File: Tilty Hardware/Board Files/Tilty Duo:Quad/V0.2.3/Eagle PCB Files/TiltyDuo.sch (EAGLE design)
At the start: 39 parts, among them U1 TEENSY_3.0_OUTER-PINS28-DIP_S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, U2 HC-09_BREAKOUT, U3 MPL3115A2LGA8, U4 LM2931, U5 MPU-6050, U6 HMC5883LSMD, U7 24LC08BT

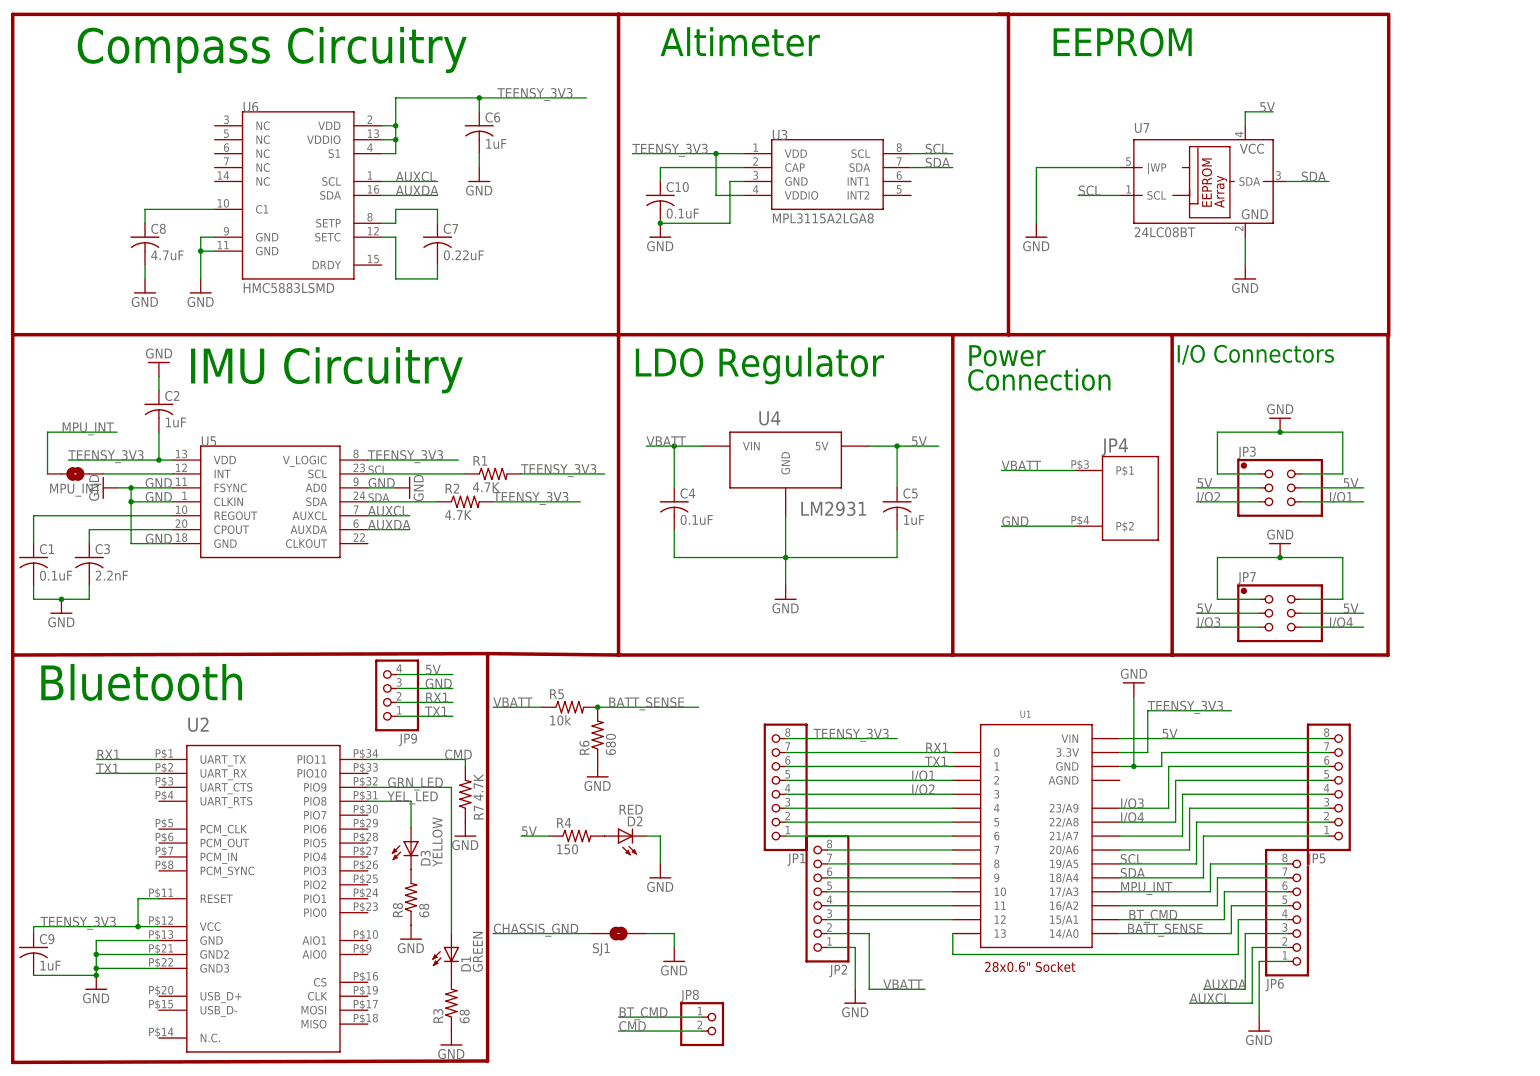
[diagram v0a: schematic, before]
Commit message: PCB hardware update
Tilty Duo/Quad v0.2.3 PCB added with minor changes.
Tilty Quad BOM updated for v0.2.2
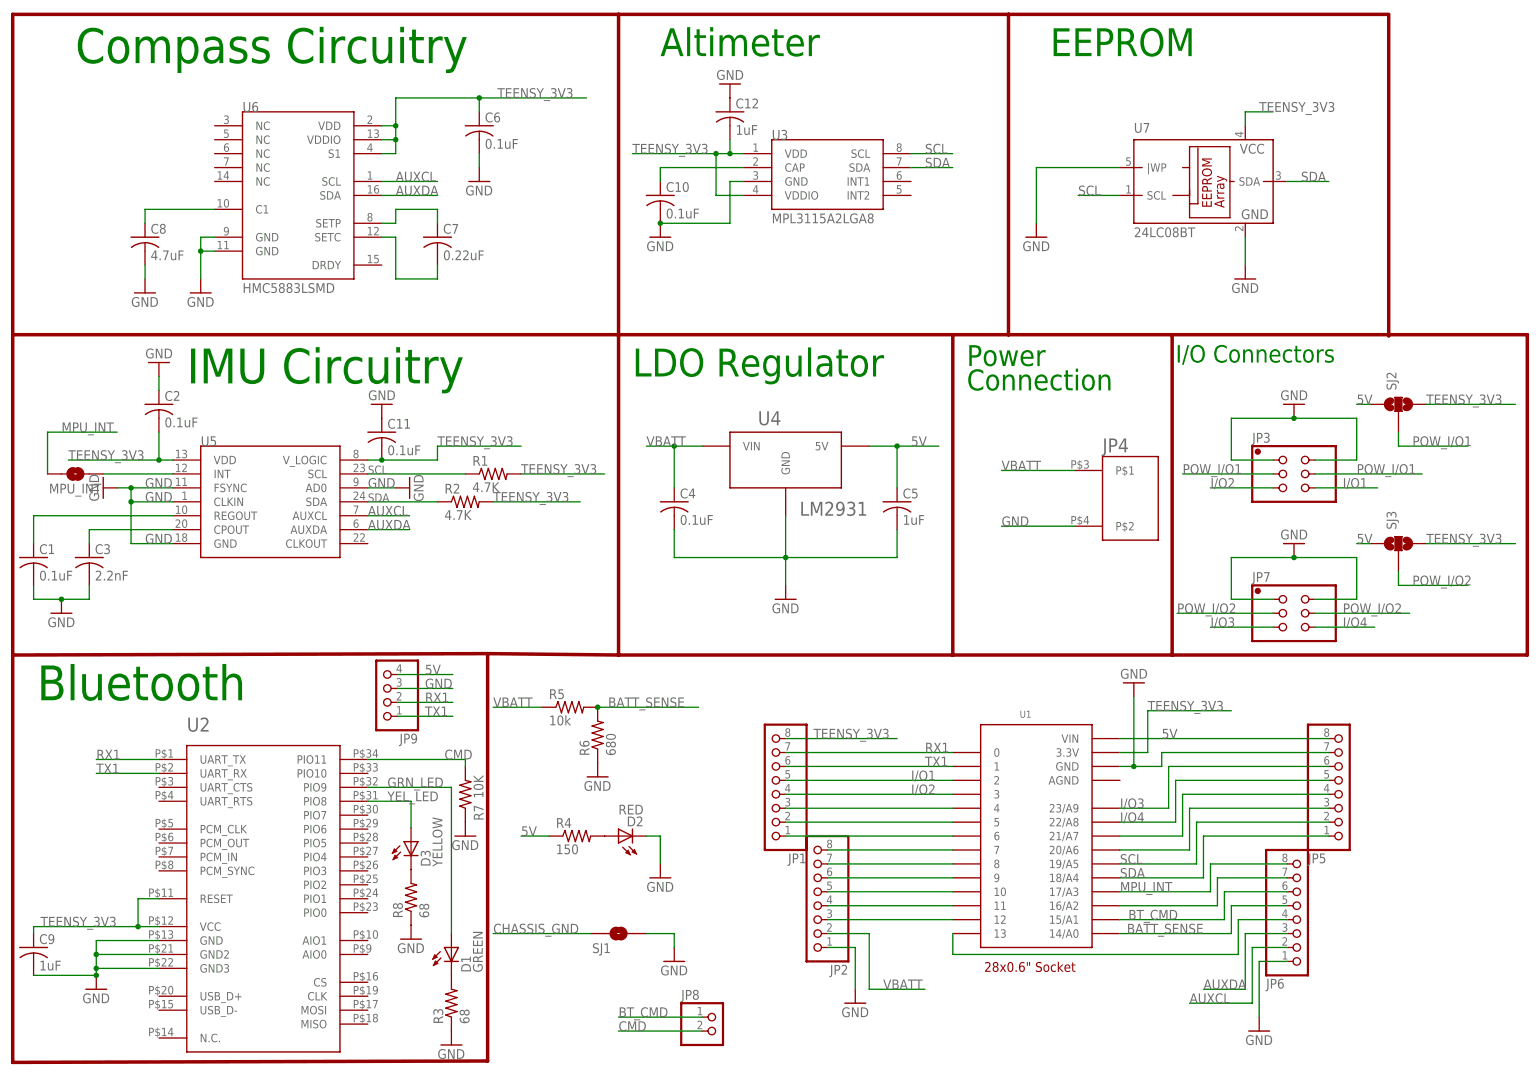
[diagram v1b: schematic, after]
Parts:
- added C11: 0.1uF, resistor:C-USC0603
- added C12: 1uF, resistor:C-USC0603
- added SJ2, SJ3: (no value), SparkFun-Passives:SOLDERJUMPER_2WAYS
- C2, C6: value 1uF -> 0.1uF
- C7, C8: ESR (none) -> <200mOhms
- R1, R2: device resistor:R-US_R0402 -> resistor:R-US_R0603
- R7: value 4.7K -> 10K
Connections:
- new net POW_I/O1: JP3.3, JP3.4, SJ2.2
- new net POW_I/O2: JP7.3, JP7.4, SJ3.2
- net 5V: now also SJ2.1, SJ3.1; no longer JP3.3, JP3.4, JP7.3, JP7.4, U7.VCC
- net GND: now also C11.1, C12.1
- net TEENSY_3V3: now also C11.2, C12.2, SJ2.3, SJ3.3, U7.VCC
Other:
- moved on the sheet: JP3, JP7

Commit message: Updated dual motor driver and Tilty Duo/Quad PCBs, added a copuple experimental arduino programs
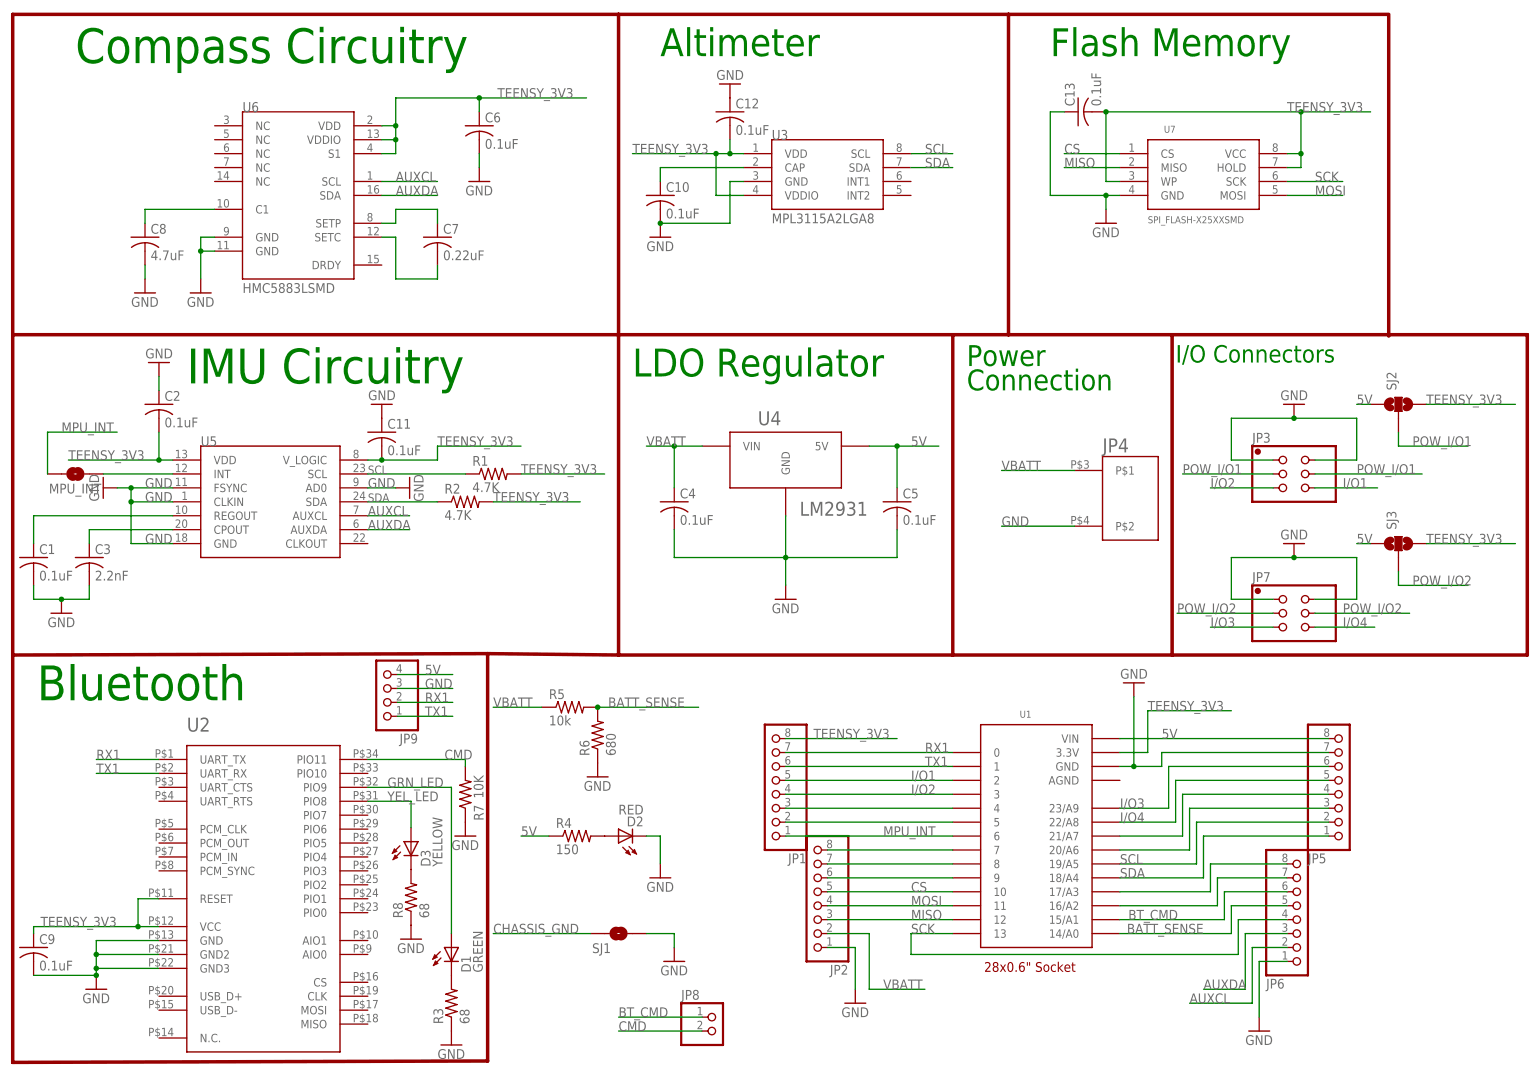
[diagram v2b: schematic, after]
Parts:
- added C13: 0.1uF, resistor:C-USC0603
- C12, C5, C9: value 1uF -> 0.1uF
- JP1, JP2, JP5, JP6: device pinhead:PINHD-1X81X08_NO_SILK -> pinhead:PINHD-1X81X08_NO_SILK_LOCK
- JP3, JP7: device pinhead:PINHD-2X32X03_NO_SILK -> pinhead:PINHD-2X32X03_NO_SS_LOCK
- U7: value 24LC08BT -> SPI_FLASH-X25XXSMD; device microchip:24LC08BT -> SparkFun-DigitalIC:SPI_FLASH-X25XXSMD; PART# (none) -> S25FL204K0TMFI011; PART#2 (none) -> S25FL208K0RMFI011
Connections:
- removed net N$13: JP2.5, U1.10
- removed net N$14: JP2.4, U1.11
- removed net N$15: JP2.3, U1.12
- removed net N$9: JP1.1, U1.6
- new net CS: JP2.5, U1.10, U7.CS
- new net MISO: JP2.3, U1.12, U7.MISO
- new net MOSI: JP2.4, U1.11, U7.MOSI
- new net SCK: JP6.4, U1.13, U7.SCK
- net GND: now also C13.1; no longer U7.|WP
- net MPU_INT: now also JP1.1, U1.6; no longer JP6.8, U1.17/A3
- net N$10: now also JP6.8, U1.17/A3; no longer JP6.4, U1.13
- net SCL: no longer U7.SCL
- net SDA: no longer U7.SDA
- net TEENSY_3V3: now also C13.2, U7.HOLD, U7.WP
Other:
- note added: "Flash Memory"
- note removed: "EEPROM"

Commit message: Slightly improved Tilty Duo/Quad PCB traces
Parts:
- JP9: device pinhead:PINHD-1X4 -> pinhead:PINHD-1X41X04_NO_SS_LOCKING
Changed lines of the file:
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@@
 <setting verticaltext="up"/>
 </settings>
-<grid distance="0.1" unitdist="inch" unit="inch" style="lines" multiple="1" display="no" altdistance="0.01" altunitdist="inch" altunit="inch"/>
+<grid distance="0.05" unitdist="inch" unit="inch" style="lines" multiple="1" display="no" altdistance="0.01" altunitdist="inch" altunit="inch"/>
 <layers>
 <layer number="1" name="Top" color="4" fill="1" visible="no" active="no"/>
@@
 <part name="GND18" library="supply1" deviceset="GND" device=""/>
 <part name="JP8" library="pinhead" deviceset="PINHD-1X2" device="1X02_NO_SILK"/>
-<part name="JP9" library="pinhead" deviceset="PINHD-1X4" device=""/>
 <part name="GND19" library="supply1" deviceset="GND" device=""/>
 <part name="R7" library="resistor" deviceset="R-US_" device="R0603" value="10K"/>
@@
 <attribute name="RATED_VOLTAGE" value="2"/>
 </part>
+<part name="JP9" library="pinhead" deviceset="PINHD-1X4" device="1X04_NO_SS_LOCKING"/>
 </parts>
 <sheets>
@@
 <instance part="GND18" gate="1" x="121.92" y="20.32"/>
 <instance part="JP8" gate="G$1" x="129.54" y="7.62"/>
-<instance part="JP9" gate="A" x="68.834" y="70.104" rot="R180"/>
 <instance part="GND19" gate="1" x="83.82" y="43.18"/>
 <instance part="R7" gate="G$1" x="83.82" y="50.8" smashed="yes" rot="R90">
@@
 <attribute name="RATED_VOLTAGE" x="195.58" y="175.26" size="1.778" layer="96" rot="R90" display="off"/>
 </instance>
+<instance part="JP9" gate="A" x="68.834" y="70.104" rot="R180"/>
 </instances>
 <busses>
@@
 </segment>
 <segment>
-<pinref part="JP9" gate="A" pin="3"/>
 <wire x1="71.374" y1="70.104" x2="81.534" y2="70.104" width="0.1524" layer="91"/>
 <label x="76.454" y="70.104" size="1.778" layer="95"/>
+<pinref part="JP9" gate="A" pin="3"/>
 </segment>
 <segment>
@@
 </net>
 <net name="TEENSY_3V3" class="3">
-<segment>
-<pinref part="R1" gate="G$1" pin="2"/>
-<wire x1="93.98" y1="109.22" x2="109.22" y2="109.22" width="0.1524" layer="91"/>
-<label x="93.98" y="109.22" size="1.778" layer="95"/>
-<wire x1="78.74" y1="114.3" x2="93.98" y2="114.3" width="0.1524" layer="91"/>
-<label x="78.74" y="114.3" size="1.778" layer="95"/>
-</segment>
 <segment>
 <pinref part="R2" gate="G$1" pin="2"/>
@@
 <wire x1="66.04" y1="111.76" x2="68.58" y2="111.76" width="0.1524" layer="91"/>
 <wire x1="68.58" y1="111.76" x2="78.74" y2="111.76" width="0.1524" layer="91"/>
+<junction x="68.58" y="111.76"/>
+<pinref part="R1" gate="G$1" pin="2"/>
+<wire x1="93.98" y1="109.22" x2="109.22" y2="109.22" width="0.1524" layer="91"/>
+<label x="93.98" y="109.22" size="1.778" layer="95"/>
+<wire x1="78.74" y1="114.3" x2="93.98" y2="114.3" width="0.1524" layer="91"/>
+<label x="78.74" y="114.3" size="1.778" layer="95"/>
 <wire x1="78.74" y1="111.76" x2="78.74" y2="114.3" width="0.1524" layer="91"/>
-<junction x="68.58" y="111.76"/>
 </segment>
 <segment>
@@
 </segment>
 <segment>
-<pinref part="JP9" gate="A" pin="4"/>
 <wire x1="71.374" y1="72.644" x2="81.534" y2="72.644" width="0.1524" layer="91"/>
 <label x="76.454" y="72.644" size="1.778" layer="95"/>
+<pinref part="JP9" gate="A" pin="4"/>
 </segment>
 <segment>
@@
 </segment>
 <segment>
-<pinref part="JP9" gate="A" pin="2"/>
 <wire x1="71.374" y1="67.564" x2="81.534" y2="67.564" width="0.1524" layer="91"/>
 <label x="76.454" y="67.564" size="1.778" layer="95"/>
+<pinref part="JP9" gate="A" pin="2"/>
 </segment>
 </net>
@@
 </segment>
 <segment>
-<pinref part="JP9" gate="A" pin="1"/>
 <wire x1="71.374" y1="65.024" x2="81.534" y2="65.024" width="0.1524" layer="91"/>
 <label x="76.454" y="65.024" size="1.778" layer="95"/>
+<pinref part="JP9" gate="A" pin="1"/>
 </segment>
 </net>
@@
 </sheet>
 </sheets>
+<errors>
+</errors>
 </schematic>
 </drawing>

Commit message: Updated Tilty Duo/Quad v0.2.3 prototype
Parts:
- D1: value GREEN -> RED
- D2: value RED -> GREEN
- R3: value 68 -> 180
- R4: value 150 -> 68
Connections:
- net GRN_LED renamed RED_LED
- removed net N$17: D2.A, R4.2
- new net N$13: D2.C, R4.1
- net 5V: now also D2.A; no longer R4.1
- net GND: now also R4.2; no longer D2.C
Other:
- moved on the sheet: D2, R4
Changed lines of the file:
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@@
 <setting verticaltext="up"/>
 </settings>
-<grid distance="0.05" unitdist="inch" unit="inch" style="lines" multiple="1" display="no" altdistance="0.01" altunitdist="inch" altunit="inch"/>
+<grid distance="0.1" unitdist="inch" unit="inch" style="lines" multiple="1" display="no" altdistance="0.01" altunitdist="inch" altunit="inch"/>
 <layers>
 <layer number="1" name="Top" color="4" fill="1" visible="no" active="no"/>
@@
 </part>
 <part name="MPU_INT" library="SparkFun-Passives" deviceset="SOLDERJUMPER" device="NO"/>
-<part name="D1" library="SparkFun-LED" deviceset="LED-GREEN" device="LED-0805_NO_SILK" value="GREEN"/>
-<part name="D2" library="SparkFun-LED" deviceset="LED-GREEN" device="LED-0805_NO_SILK" value="RED"/>
+<part name="D1" library="SparkFun-LED" deviceset="LED-GREEN" device="LED-0805_NO_SILK" value="RED"/>
+<part name="D2" library="SparkFun-LED" deviceset="LED-GREEN" device="LED-0805_NO_SILK" value="GREEN"/>
 <part name="GND16" library="supply1" deviceset="GND" device=""/>
-<part name="R4" library="resistor" deviceset="R-US_" device="R0603" value="150"/>
 <part name="GND17" library="supply1" deviceset="GND" device=""/>
 <part name="C9" library="resistor" deviceset="C-US" device="C0603" value="0.1uF">
@@
 </part>
 <part name="GND20" library="SparkFun" deviceset="GND" device=""/>
-<part name="R3" library="resistor" deviceset="R-US_" device="R0603" value="68"/>
+<part name="R3" library="resistor" deviceset="R-US_" device="R0603" value="180"/>
 <part name="GND21" library="supply1" deviceset="GND" device=""/>
 <part name="D3" library="SparkFun-LED" deviceset="LED-GREEN" device="LED-0805_NO_SILK" value="YELLOW"/>
@@
 </part>
 <part name="JP9" library="pinhead" deviceset="PINHD-1X4" device="1X04_NO_SS_LOCKING"/>
+<part name="R4" library="resistor" deviceset="R-US_" device="R0603" value="68"/>
 </parts>
 <sheets>
@@
 </instance>
 <instance part="D1" gate="G$1" x="81.28" y="22.86"/>
-<instance part="D2" gate="G$1" x="111.76" y="43.18" rot="R90"/>
+<instance part="D2" gate="G$1" x="101.6" y="43.18" rot="R90"/>
 <instance part="GND16" gate="1" x="81.28" y="5.08"/>
-<instance part="R4" gate="G$1" x="104.14" y="43.18"/>
 <instance part="GND17" gate="1" x="119.38" y="35.56"/>
 <instance part="C9" gate="G$1" x="5.08" y="22.86">
@@
 </instance>
 <instance part="JP9" gate="A" x="68.834" y="70.104" rot="R180"/>
+<instance part="R4" gate="G$1" x="114.3" y="43.18"/>
 </instances>
 <busses>
@@
 </segment>
 <segment>
-<pinref part="D2" gate="G$1" pin="C"/>
-<wire x1="116.84" y1="43.18" x2="119.38" y2="43.18" width="0.1524" layer="91"/>
 <wire x1="119.38" y1="43.18" x2="119.38" y2="38.1" width="0.1524" layer="91"/>
 <pinref part="GND17" gate="1" pin="GND"/>
+<pinref part="R4" gate="G$1" pin="2"/>
 </segment>
 <segment>
@@
 </segment>
 <segment>
-<pinref part="R4" gate="G$1" pin="1"/>
 <wire x1="99.06" y1="43.18" x2="93.98" y2="43.18" width="0.1524" layer="91"/>
 <label x="93.98" y="43.18" size="1.778" layer="95"/>
+<pinref part="D2" gate="G$1" pin="A"/>
 </segment>
 <segment>
@@
 </segment>
 </net>
-<net name="N$17" class="0">
-<segment>
-<pinref part="D2" gate="G$1" pin="A"/>
-<pinref part="R4" gate="G$1" pin="2"/>
-</segment>
-</net>
 <net name="CHASSIS_GND" class="0">
 <segment>
@@
 </segment>
 </net>
-<net name="GRN_LED" class="0">
+<net name="RED_LED" class="0">
 <segment>
 <pinref part="U2" gate="G$1" pin="PIO9"/>
@@
 </segment>
 </net>
+<net name="N$13" class="0">
+<segment>
+<pinref part="D2" gate="G$1" pin="C"/>
+<pinref part="R4" gate="G$1" pin="1"/>
+<wire x1="109.22" y1="43.18" x2="106.68" y2="43.18" width="0.1524" layer="91"/>
+</segment>
+</net>
